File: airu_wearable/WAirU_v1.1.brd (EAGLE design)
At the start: 40.3 x 50 mm, 66 parts, among them J2 2p-2.0, Q2 MMBT3904LT1G, Q3 MMBT3904LT1G, Q4 BSS84, Q6 BSS84, U1 MOLEX-53261-0871, U2 CN3065-DFN8, U3 HDC1080DMBT, U4 CJT1117-3.3-SOT223, U5 CH340T-SSOP20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

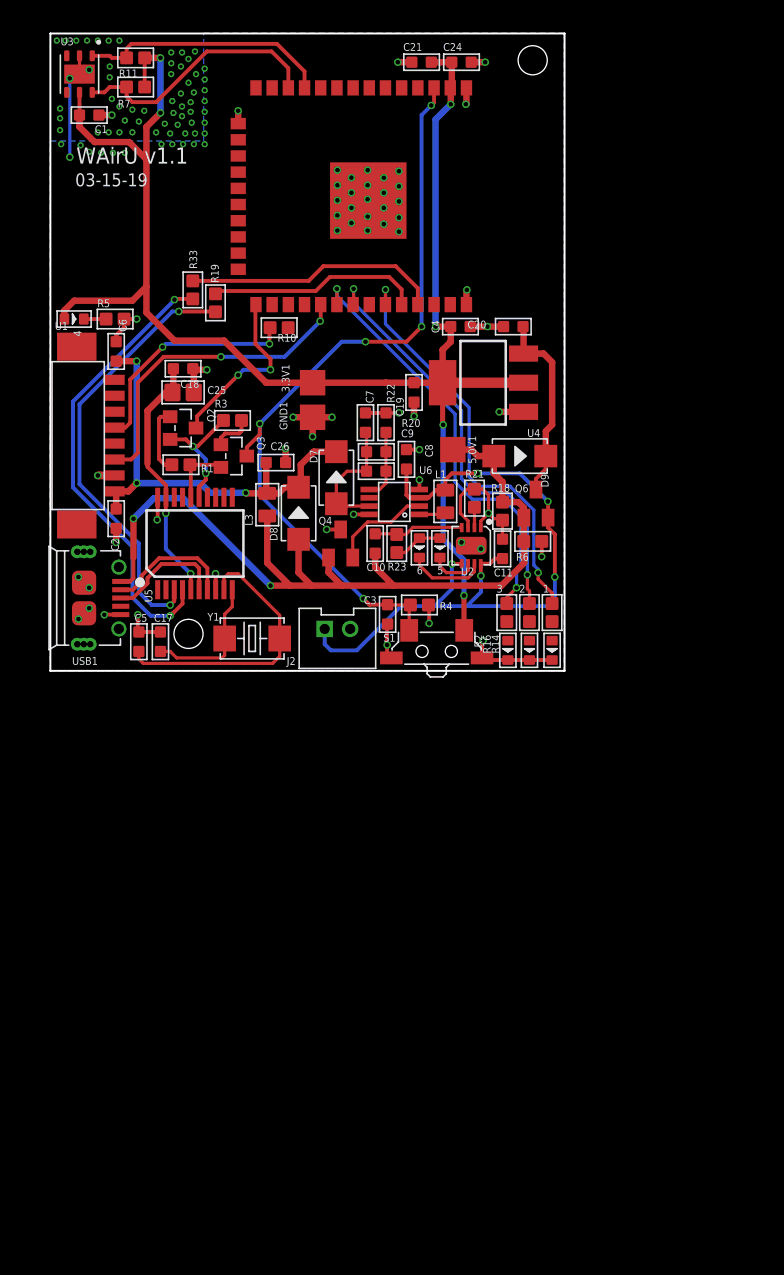
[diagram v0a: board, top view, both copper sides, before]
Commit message: Remove USB-TTL chip, flashing uses PM port, re-arrange according to Housing_bottomV1
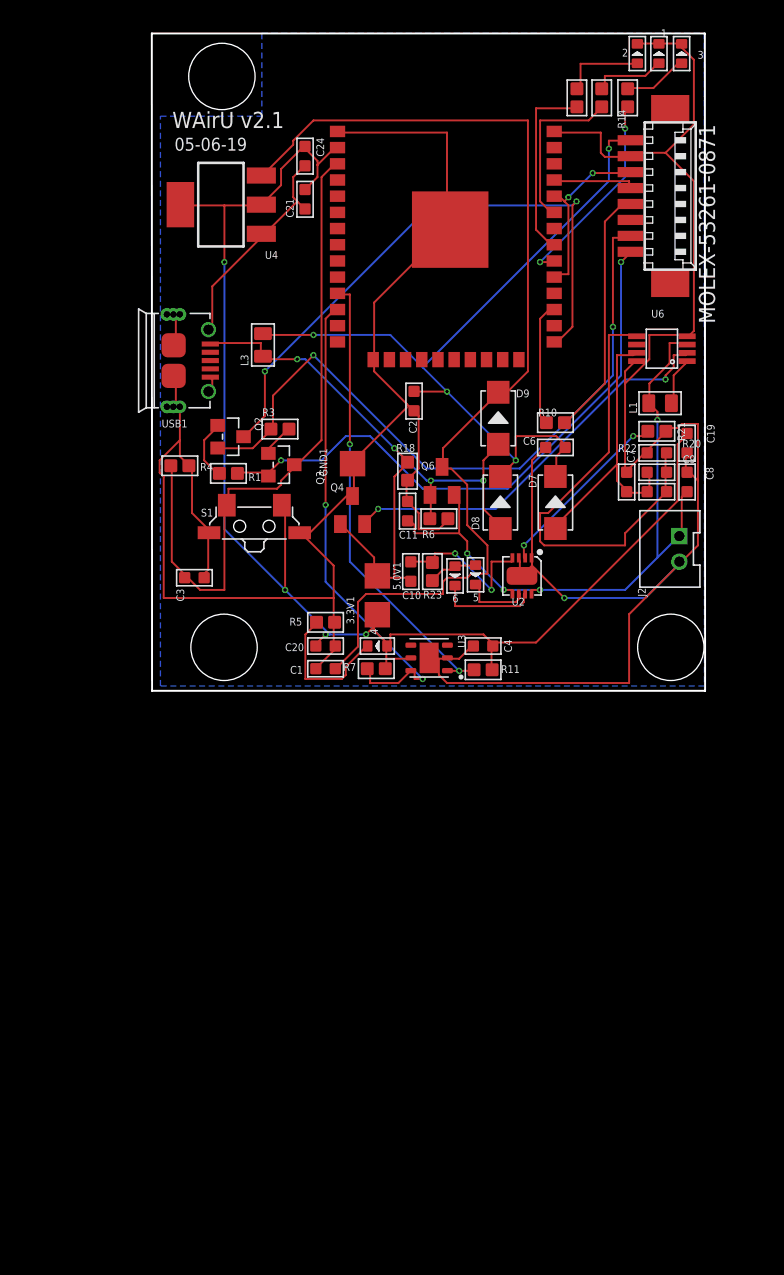
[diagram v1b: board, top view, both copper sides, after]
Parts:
- removed C17, C5: 22pf, Seeed-Capacitor:C0603
- removed C18: 100nf, Seeed-Capacitor:C0603
- removed C25: 22uf, Seeed-Capacitor:C0805
- removed C26: 10uf, Seeed-Capacitor:C0603
- removed R19, R33: 220R, Seeed-Resistor:R0603
- removed U1: MOLEX-53261-0871, Molex_53261_0871_Connector:MOLEX-53261-0871
- removed U5: CH340T-SSOP20, Seeed-IC:SSOP20-0.65-7.6X5.2MM
- removed Y1: 12MHZ, Seeed-Crystal Oscillator:X2-SMD-5.0X3.2X1.3MM
- added MOLEX-53261-0871: 53261-08, con-molex:53261-08
- moved R11 55.2 mm to (33.9, 0.08)
- moved U3 53.4 mm to (29.7, 1.02), turned to 180 degrees
- moved R7 49.4 mm to (25.6, 0.17)
- moved 3 48.8 mm to (49.5, 48.4), turned to 90 degrees
- moved 2 47.6 mm to (46.0, 48.4), turned to 90 degrees
- moved 1 47.6 mm to (47.7, 48.4), turned to 90 degrees
- moved C1 45.6 mm to (21.6, 1.95)
- moved R2 41.5 mm to (45.3, 45.0), turned to 0 degrees
- moved R14 40.6 mm to (43.3, 45.0), turned to 0 degrees
- moved R16 40.6 mm to (41.3, 45.0), turned to 0 degrees
- moved C6 35.3 mm to (39.6, 17.5), turned to 90 degrees
- moved 4 35.0 mm to (25.7, 1.95), turned to 180 degrees
- moved C20 30.6 mm to (21.6, 0.17)
- moved R5 29.0 mm to (21.6, 3.81)
- moved J2 27.0 mm to (48.6, 9.57), turned to 270 degrees
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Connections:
- removed net N$20: R10.2, U1.TXD
- removed net N$24: U5.7, USB1.2
- removed net N$25: U5.6, USB1.3
- removed net N$26: C5.2, U5.9, Y1.2
- removed net N$27: C17.2, U5.10, Y1.1
- removed net N$28: R19.2, U5.3
- removed net N$33: R33.2, U7.35
- removed net RXD0: R19.1, U7.34
- removed net TXD0: R33.1, U5.4
- new net RXD: MOLEX-53261-0871.5, U7.35
- new net TXD: MOLEX-53261-0871.4, R10.2
- net 3.3V: no longer C18.2, C25.1, U5.19, U5.5
- net 5.0V: now also MOLEX-53261-0871.8; no longer C26.2, U1.5V
- net DTR: now also MOLEX-53261-0871.2; no longer U5.15
- net GND: now also MOLEX-53261-0871.7; no longer C17.1, C18.1, C25.2, C26.1, C5.1, U1.GND, U5.20, U5.8
- net PM_RESET: now also MOLEX-53261-0871.3; no longer U1.RESET
- net PM_SET: now also MOLEX-53261-0871.6, U7.34; no longer U1.SET
- net RTS: now also MOLEX-53261-0871.1; no longer U5.16
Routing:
- net GND: track 76.4 -> 275.5 mm, vias 63 -> 1
- net N$8: track 15.2 -> 81.0 mm
- net DTR: track 9.88 -> 54.5 mm
- net RTS: track 5.10 -> 47.0 mm, vias 0 -> 2
- net TXD0: track 36.1 -> 0.00 mm, vias 2 -> 0
- net N$28: track 34.6 -> 0.00 mm, vias 2 -> 0
- net GPIO0: track 13.9 -> 47.8 mm
- net N$10: track 5.51 -> 36.5 mm
- net 3.3V: track 141.5 -> 111.8 mm, vias 8 -> 4
- net 5.0V: track 35.4 -> 62.6 mm, vias 3 -> 4
- net N$4: track 7.85 -> 31.7 mm, vias 0 -> 2
- net N$26: track 22.0 -> 0.00 mm
- net N$33: track 20.1 -> 0.00 mm
- net TXD: track 0.00 -> 19.7 mm
- net STAT_LED1: track 32.7 -> 13.2 mm, vias 2 -> 0
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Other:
- board size 40.3 x 50 mm -> 43.4 x 51.6 mm
- board text added: "05-06-19"
- board text added: "WAirU v2.1"
- board text removed: "03-15-19"
- board text removed: "WAirU v1.1"

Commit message: changed PM_SET to GPIO4
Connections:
- net PM_SET: now also U7.26; no longer U7.29

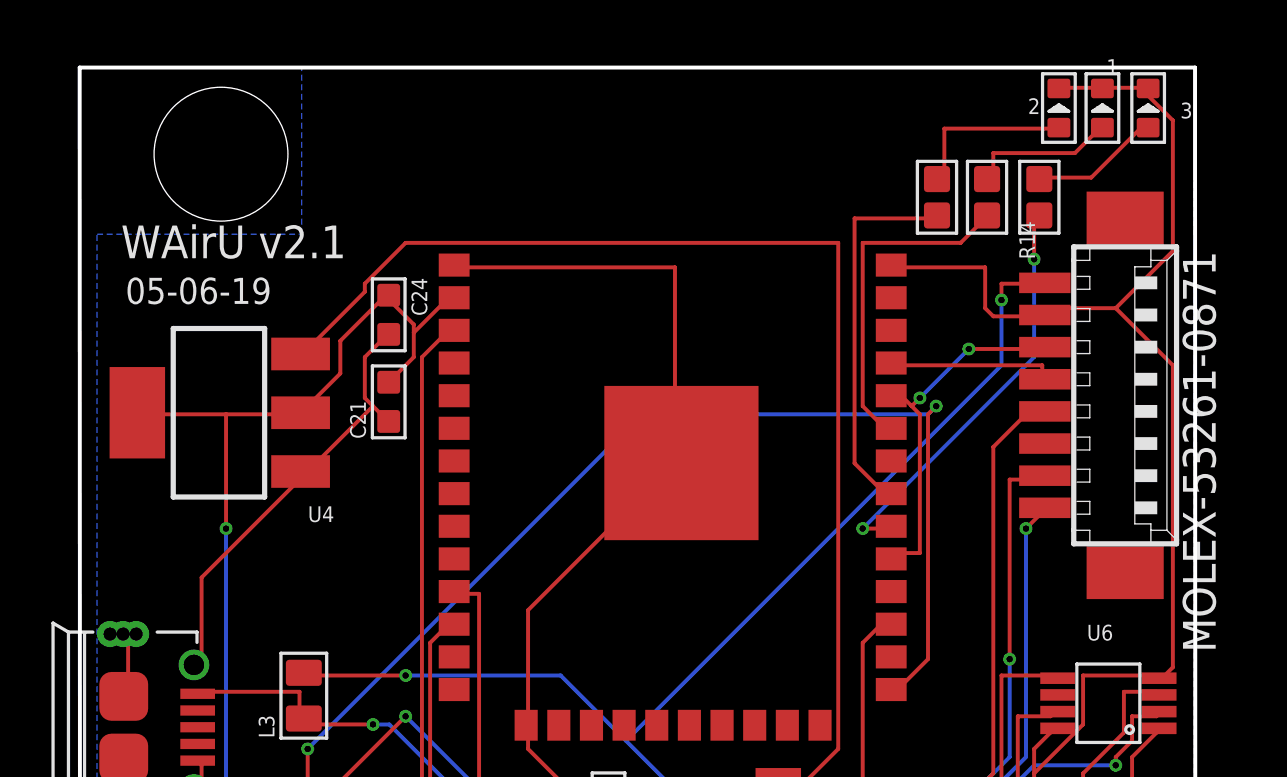
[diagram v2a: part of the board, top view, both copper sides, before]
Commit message: routed PM_RESET and added dimensions, removed GND polygon from upper left
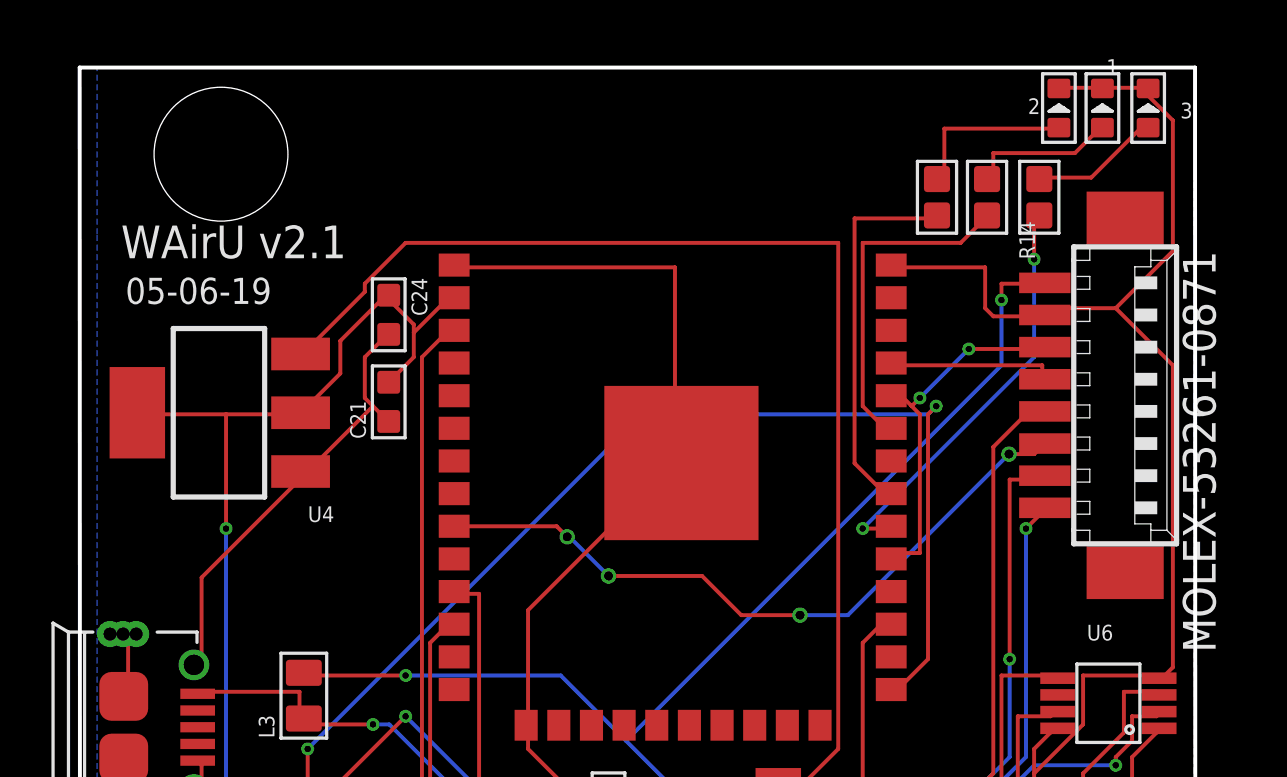
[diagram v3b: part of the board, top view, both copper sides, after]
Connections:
- net PM_RESET: now also U7.9
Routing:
- net PM_RESET: track 0.00 -> 27.2 mm, vias 0 -> 4
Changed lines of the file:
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@@
 <dimension x1="7.977759375" y1="-1.5661625" x2="7.957871875" y2="24.296903125" x3="-0.07555625" y3="11.359184375" textsize="1.778" layer="1" dtype="diameter"/>
 <dimension x1="51.36319375" y1="-1.5661625" x2="51.30286875" y2="50.032996875" x3="58.104690625" y3="24.241334375" textsize="1.778" layer="1" dtype="diameter"/>
+<dimension x1="7.957871875" y1="-1.523846875" x2="48.673696875" y2="1.845840625" x3="28.315784375" y3="-5.75675625" textsize="1.778" layer="1" dtype="horizontal"/>
+<dimension x1="7.957871875" y1="-1.60850625" x2="13.62519375" y2="1.845846875" x3="10.79153125" y3="-4.06359375" textsize="1.778" layer="1" dtype="horizontal"/>
+<dimension x1="7.957871875" y1="50.032996875" x2="13.45588125" y2="46.63003125" x3="10.706875" y3="50.9642375" textsize="1.778" layer="1" dtype="horizontal"/>
+<dimension x1="13.460653125" y1="46.64666875" x2="11.68283125" y2="50.032996875" x3="-0.423290625" y3="48.33983125" textsize="1.778" layer="1" dtype="vertical"/>
+<dimension x1="13.62996875" y1="1.86248125" x2="13.62996875" y2="-1.60850625" x3="-4.57154375" y3="0.1269875" textsize="1.778" layer="1" dtype="diameter"/>
 </plain>
 <attributes>
@@
 <vertex x="8.635134375" y="-1.18521875"/>
 <vertex x="8.635134375" y="43.514315625"/>
-<vertex x="16.593009375" y="43.514315625"/>
-<vertex x="16.593009375" y="50.032996875"/>
+<vertex x="8.635140625" y="43.514315625"/>
+<vertex x="8.635140625" y="50.032996875"/>
 <vertex x="51.30286875" y="50.032996875"/>
 <vertex x="51.30286875" y="-1.18521875"/>
@@
 <signal name="PM_RESET">
 <contactref element="MOLEX-53261-0871" pad="3"/>
+<contactref element="U7" pad="9"/>
+<wire x1="45.501190625" y1="35.374609375" x2="45.09041875" y2="34.9638375" width="0.1524" layer="1"/>
+<wire x1="45.09041875" y1="34.9638375" x2="44.106921875" y2="34.9638375" width="0.1524" layer="1"/>
+<via x="44.106921875" y="34.9638375" extent="1-16" drill="0.35"/>
+<wire x1="44.106921875" y1="34.9638375" x2="37.842215625" y2="28.69913125" width="0.1524" layer="16"/>
+<wire x1="37.842215625" y1="28.69913125" x2="35.979734375" y2="28.69913125" width="0.1524" layer="16"/>
+<via x="35.979734375" y="28.69913125" extent="1-16" drill="0.35"/>
+<wire x1="35.979734375" y1="28.69913125" x2="33.6939625" y2="28.69913125" width="0.1524" layer="1"/>
+<wire x1="33.6939625" y1="28.69913125" x2="32.170115625" y2="30.222978125" width="0.1524" layer="1"/>
+<wire x1="32.170115625" y1="30.222978125" x2="28.5298125" y2="30.222978125" width="0.1524" layer="1"/>
+<via x="28.5298125" y="30.222978125" extent="1-16" drill="0.35"/>
+<wire x1="28.5298125" y1="30.222978125" x2="27.005965625" y2="31.746825" width="0.1524" layer="16"/>
+<wire x1="27.005965625" y1="31.746825" x2="26.92130625" y2="31.746825" width="0.1524" layer="16"/>
+<via x="26.92130625" y="31.746825" extent="1-16" drill="0.35"/>
+<wire x1="26.92130625" y1="31.746825" x2="26.51205" y2="32.15608125" width="0.1524" layer="1"/>
+<wire x1="26.51205" y1="32.15608125" x2="22.5259625" y2="32.15608125" width="0.1524" layer="1"/>
 </signal>
 <signal name="PM_SET">

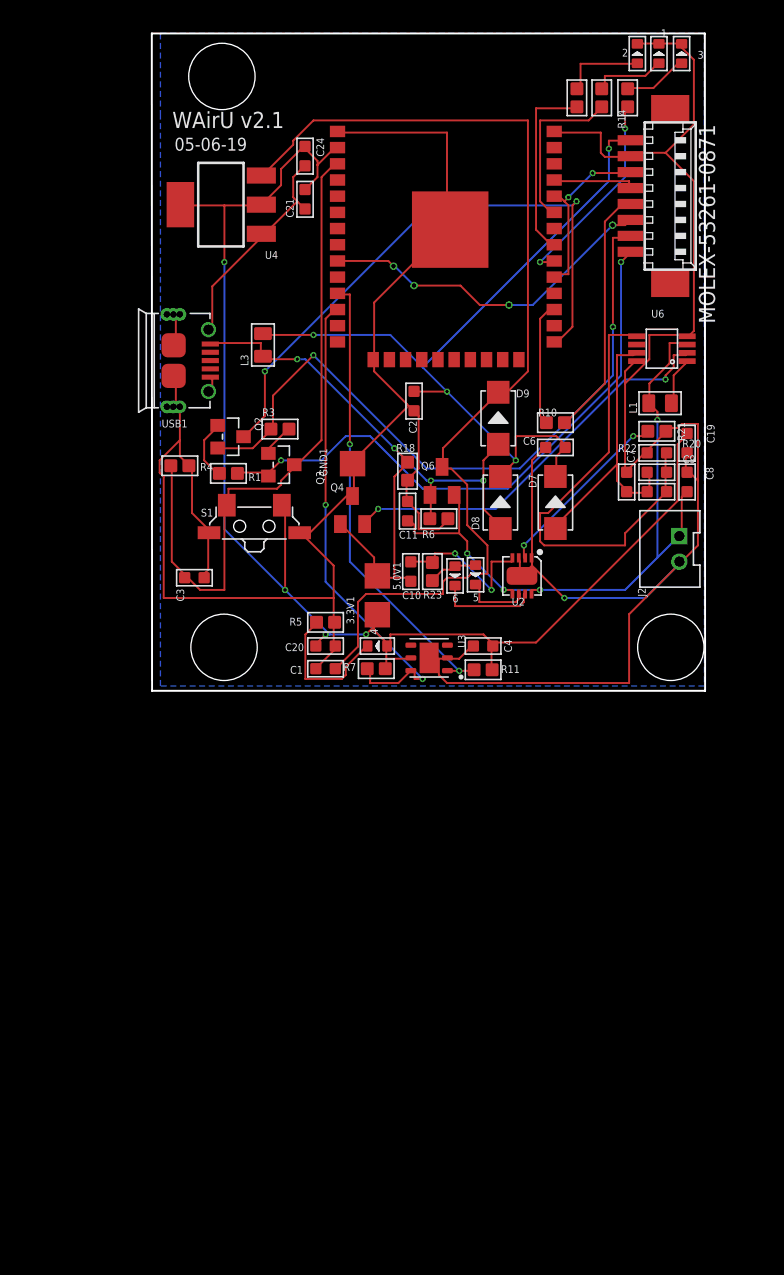
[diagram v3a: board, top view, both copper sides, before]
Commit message: - Remove led - Re-position Status Led 1 near the button - Replace reset button with SMD one - Route GND signal to ground plan - Add heat dissipation surrounding the temperature sensor - Remove ground plane copper pour from temperature sensor - Adjust board dimension, mounting holes dimention and position
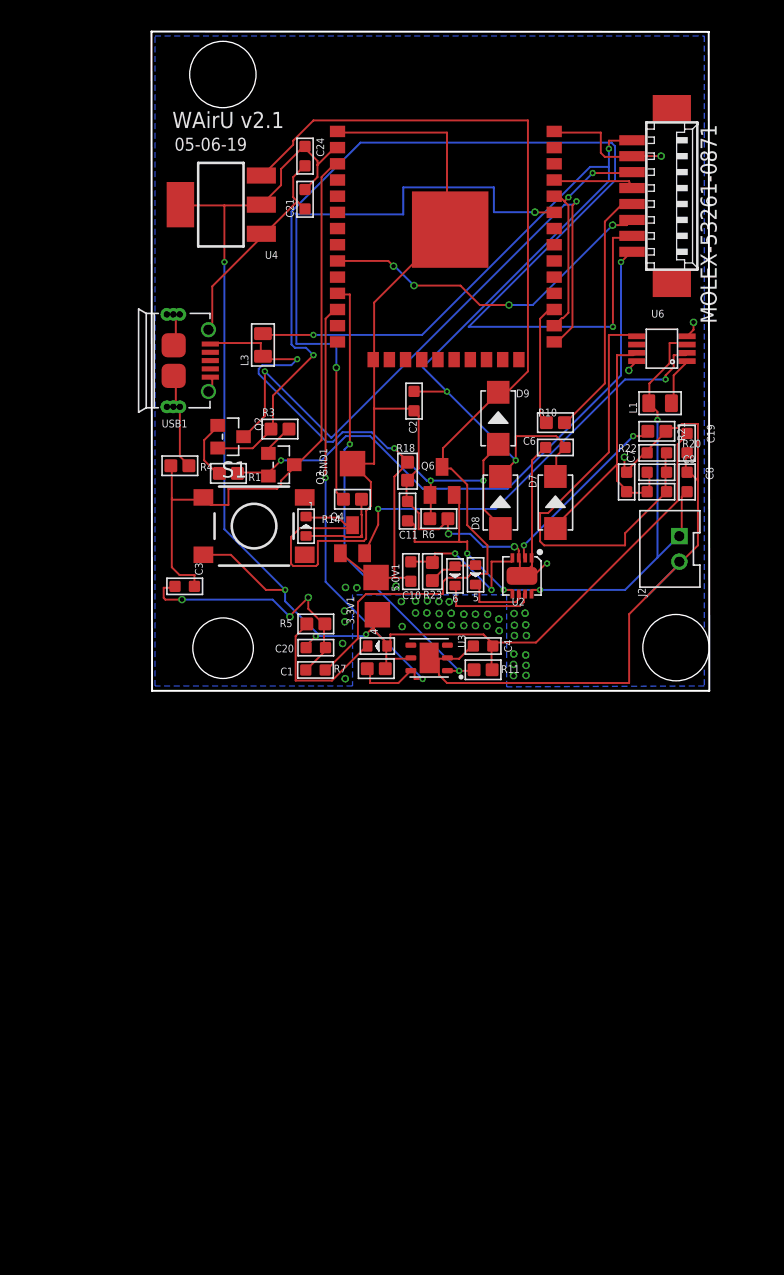
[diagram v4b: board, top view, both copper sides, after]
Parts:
- removed 2: GREEN-0603, Seeed-LED:LED-0603
- removed 3: BLUE-0603, Seeed-LED:LED-0603
- removed R16: 10R, Seeed-Resistor:R0603
- removed R2: 100R, Seeed-Resistor:R0603
- S1: value TS-1188E -> DTSM-6; device OPL_Switch:SW4-SMD-7.0X3.5X3.5MM-90D -> switch-tact:DTSM-6
- moved 1 46.3 mm to (20.1, 11.3)
- moved R14 37.1 mm to (23.7, 13.5), turned to 270 degrees
- moved Q4 2.29 mm to (23.7, 10.3)
- moved C3 1.02 mm to (10.5, 6.63), turned to 90 degrees
- moved C20 0.79 mm to (20.8, 0.07)
- moved R5 0.77 mm to (20.8, 3.68)
- moved C1 0.77 mm to (20.8, 1.82)
- moved 5.0V1 0.16 mm to (25.5, 7.32)
- moved MOLEX-53261-0871 0.13 mm to (48.1, 37.2)
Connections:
- removed net N$1: 2.+, R16.1
- removed net N$22: 3.+, R2.1
- net 3.3V: now also S1.3; no longer S1.2
- net GND: no longer 2.-, 3.-, S1.S1, S1.S2
- net STAT_LED2: no longer R16.2
- net STAT_LED3: no longer R2.2
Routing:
- net GND: track 275.5 -> 227.0 mm, vias 1 -> 10
- net STAT_LED1: track 13.2 -> 50.4 mm, vias 0 -> 2
- net DTR: track 54.5 -> 91.1 mm
- net 5.0V: track 62.6 -> 81.8 mm
- net STAT_LED3: track 16.2 -> 0.18 mm, vias 2 -> 0
- net STAT_LED2: track 14.8 -> 0.18 mm
- net N$1: track 6.68 -> 0.00 mm, vias 0 -> 10
- net VBUS: track 56.4 -> 61.5 mm
- net N$22: track 5.04 -> 0.00 mm, vias 0 -> 1
- net GPIO0: track 47.8 -> 52.1 mm
- net RESET: track 52.3 -> 48.4 mm
- net PM_SET: track 14.1 -> 17.8 mm
- net N$4: track 31.7 -> 33.8 mm
- net N$7: track 5.85 -> 7.49 mm
- net 3.3V: track 111.8 -> 113.2 mm
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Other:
- board size 43.4 x 51.6 mm -> 43.8 x 51.7 mm

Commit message: removed ground traces and added ground poly pour on top layer
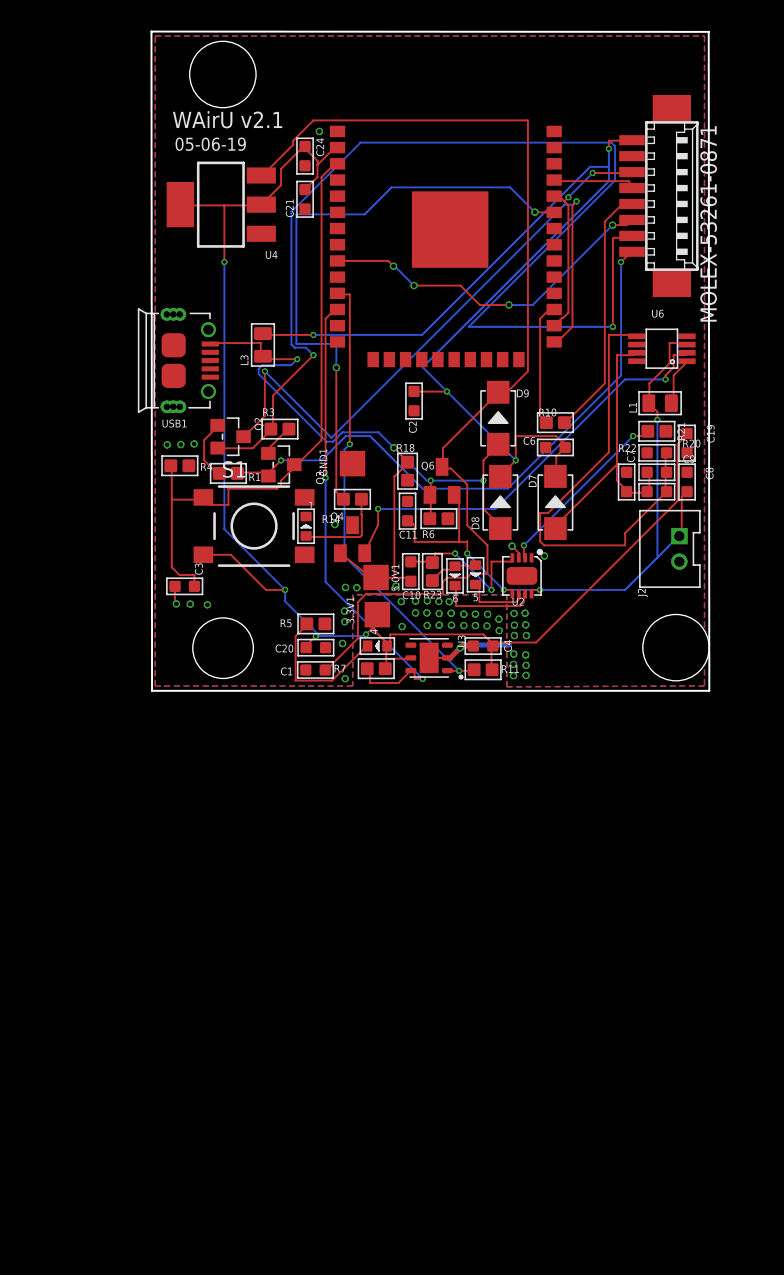
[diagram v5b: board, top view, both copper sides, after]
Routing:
- net GND: track 227.0 -> 10.4 mm, vias 10 -> 11
- net STAT_LED1: track 50.4 -> 47.6 mm
- added copper zone on layer 1, net GND
